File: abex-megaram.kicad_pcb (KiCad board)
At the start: 2 copper layers, 135.5 x 71.5 mm, 54 parts, among them P1 0877159106, P2 CONN_01X01, P3 CONN_01X01, P4 CONN_01X01, P5 CONN_01X01, P6 CONN_01X01, SW2 SW_Push, U1 74HC04, U14 STM32F407VGTx, U7 ISSI61WV5128BL, U8 ISSI61WV5128BL

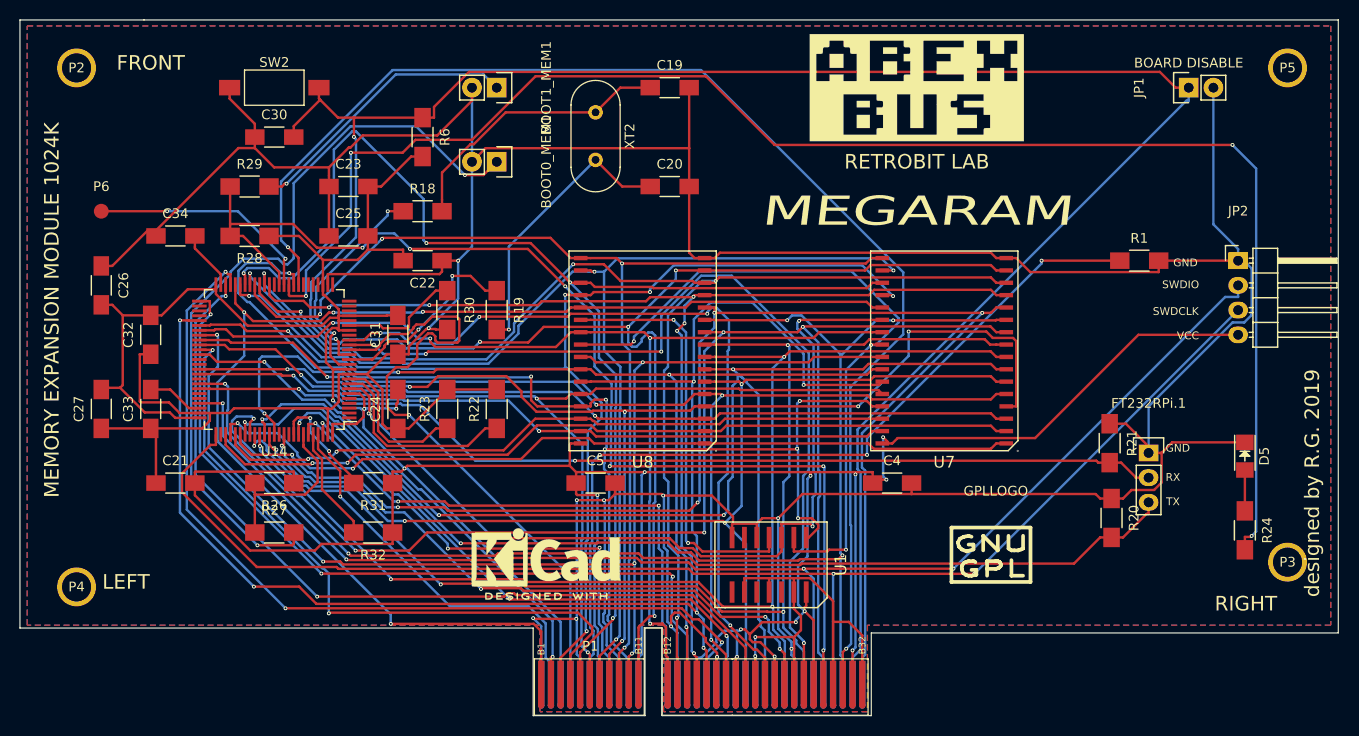
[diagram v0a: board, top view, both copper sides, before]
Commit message: Added a three channel dip-switch for select configuration
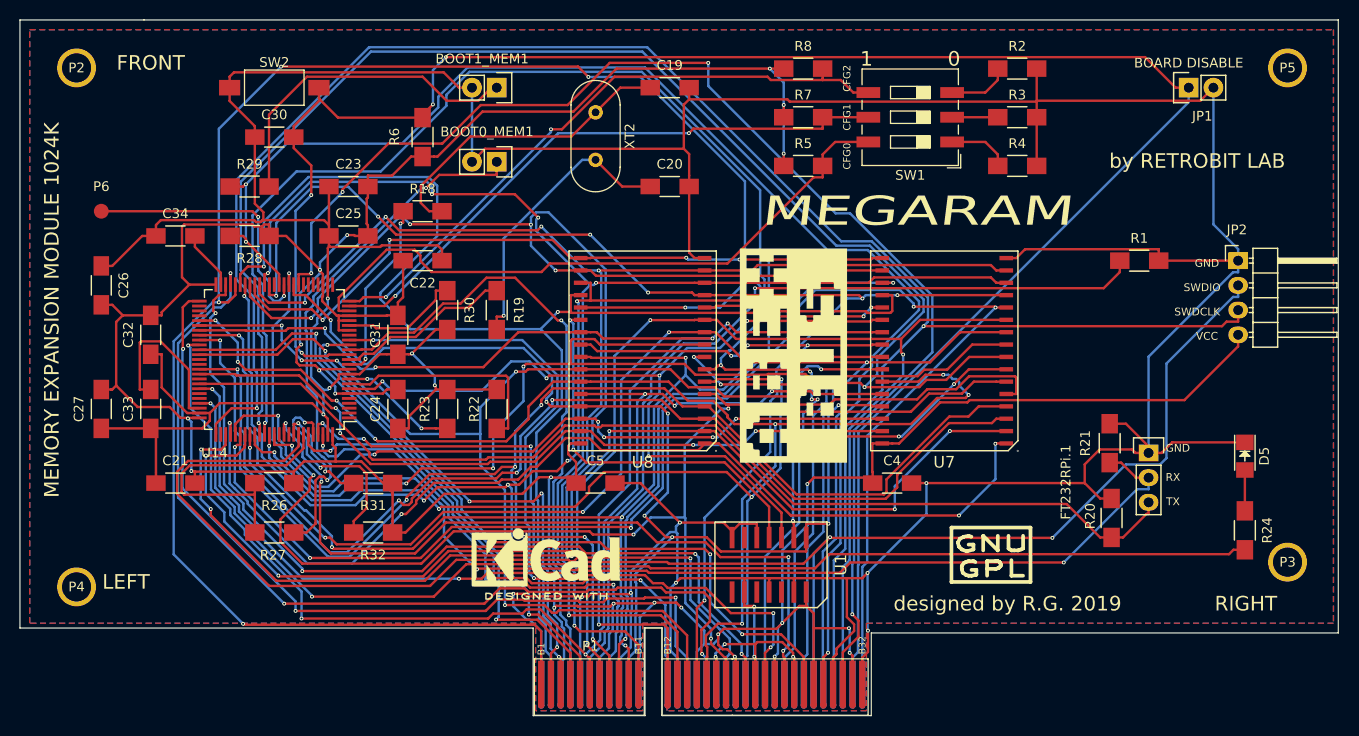
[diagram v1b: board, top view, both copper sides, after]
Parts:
- added R2: 470, Resistors_SMD:R_1206_HandSoldering, F.Cu at (180.5, 59.0)
- added R3: 470, Resistors_SMD:R_1206_HandSoldering, F.Cu at (180.5, 64.0)
- added R4: 470, Resistors_SMD:R_1206_HandSoldering, F.Cu at (180.5, 69.0)
- added R5: 4.7K, Resistors_SMD:R_1206_HandSoldering, F.Cu at (158.5, 69.0)
- added R7: 4.7K, Resistors_SMD:R_1206_HandSoldering, F.Cu at (158.5, 64.0)
- added R8: 4.7K, Resistors_SMD:R_1206_HandSoldering, F.Cu at (158.5, 59.0)
- added SW1: SW_DIP_x03, RetroBitLab:SW_DIP_SPSTx03_Slide_9.78x9.8mm_W8.61mm_P2.54mm, F.Cu at (169.5, 64.0)
- moved ABEXLOGO 30.3 mm to (157.5, 88.5), turned to 90 degrees
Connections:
- U14 pad 23: (no net) -> mCONF0
- U14 pad 24: (no net) -> mCONF1
- U14 pad 25: (no net) -> mCONF2
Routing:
- net mD7: track 131.9 -> 203.6 mm, vias 4 -> 8
- net mCONF0: track 0.00 -> 67.1 mm
- net mA4: track 127.1 -> 193.7 mm, vias 4 -> 5
- net mCONF2: track 0.00 -> 64.9 mm, vias 0 -> 2
- net mCONF1: track 0.00 -> 62.1 mm, vias 0 -> 2
- net SWDCLK: track 142.2 -> 195.1 mm
- net mA5: track 134.7 -> 177.3 mm, vias 4 -> 8
- net LEDGRN_MEM: track 159.8 -> 128.9 mm, vias 4 -> 2
- net mB2: track 84.5 -> 115.3 mm, vias 2 -> 6
- net ~mD1XX: track 60.2 -> 89.8 mm, vias 3 -> 1
- net mB0: track 85.5 -> 113.9 mm, vias 2 -> 4
- net mRD5: track 116.2 -> 143.6 mm, vias 6 -> 3
- net mA13: track 104.7 -> 130.3 mm, vias 3 -> 6
- net Net-(BOOT0_MEM1-Pad1): track 78.7 -> 54.4 mm
- net mD6: track 118.7 -> 142.4 mm, vias 5 -> 3
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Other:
- board text added: "0"
- board text added: "1"
- board text added: "CFG0"
- board text added: "CFG1"
- board text added: "CFG2"
- board text added: "by RETROBIT LAB"
- board text removed: "RETROBIT LAB"

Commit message: Optimized for 8 bit access. Added a configuration option. A31 on connector is 5VDC. Not used here
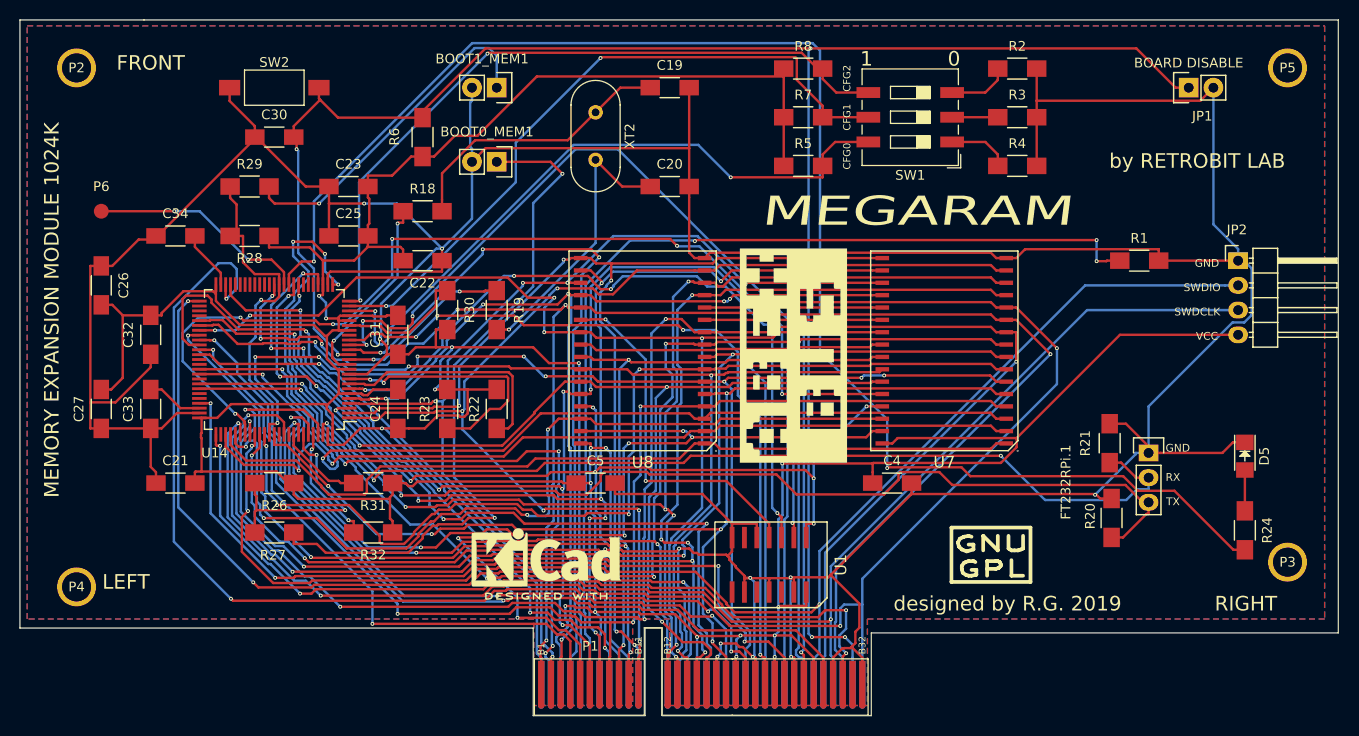
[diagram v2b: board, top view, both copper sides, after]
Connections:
- P1 pad A31: VCC_3V3 -> (no net)
- U14 pad 1: (no net) -> mD2
- U14 pad 2: (no net) -> mD3
- U14 pad 26: (no net) -> ~mRST
- U14 pad 29: (no net) -> ~mREF
- U14 pad 3: (no net) -> mD4
- U14 pad 38: (no net) -> mD7
- U14 pad 39: mD0 -> (no net)
- U14 pad 4: (no net) -> mD5
- U14 pad 40: mD1 -> (no net)
- U14 pad 41: mD2 -> (no net)
- U14 pad 42: mD3 -> (no net)
- U14 pad 43: mD4 -> (no net)
- U14 pad 44: mD5 -> (no net)
- U14 pad 45: mD6 -> (no net)
- U14 pad 46: mD7 -> (no net)
- U14 pad 5: (no net) -> mD6
- U14 pad 97: ~mRST -> mD0
- U14 pad 98: ~mREF -> mD1
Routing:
- net mD7: track 203.6 -> 115.1 mm, vias 8 -> 6
- net SWDCLK: track 195.1 -> 142.2 mm, vias 2 -> 3
- net mA4: track 193.7 -> 144.1 mm
- net GND: track 592.3 -> 641.8 mm, vias 18 -> 16
- net ~mCCTL: track 133.8 -> 87.8 mm
- net mA5: track 177.3 -> 135.4 mm, vias 8 -> 5
- net mD6: track 142.4 -> 101.4 mm, vias 3 -> 6
- net mRD5: track 143.6 -> 104.6 mm, vias 3 -> 2
- net mA2: track 136.3 -> 171.4 mm
- net ~mRST: track 49.2 -> 82.5 mm, vias 3 -> 7
- net ~mS5: track 72.8 -> 102.2 mm
- net mB2: track 115.3 -> 87.5 mm, vias 6 -> 2
- net mB1: track 77.9 -> 105.1 mm, vias 4 -> 6
- net LEDGRN_MEM: track 128.9 -> 155.5 mm
- net mD1: track 143.6 -> 118.5 mm, vias 5 -> 6
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
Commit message: Upgraded to a dual chip select for external SRAM. In this case up to 1536k can be addressable
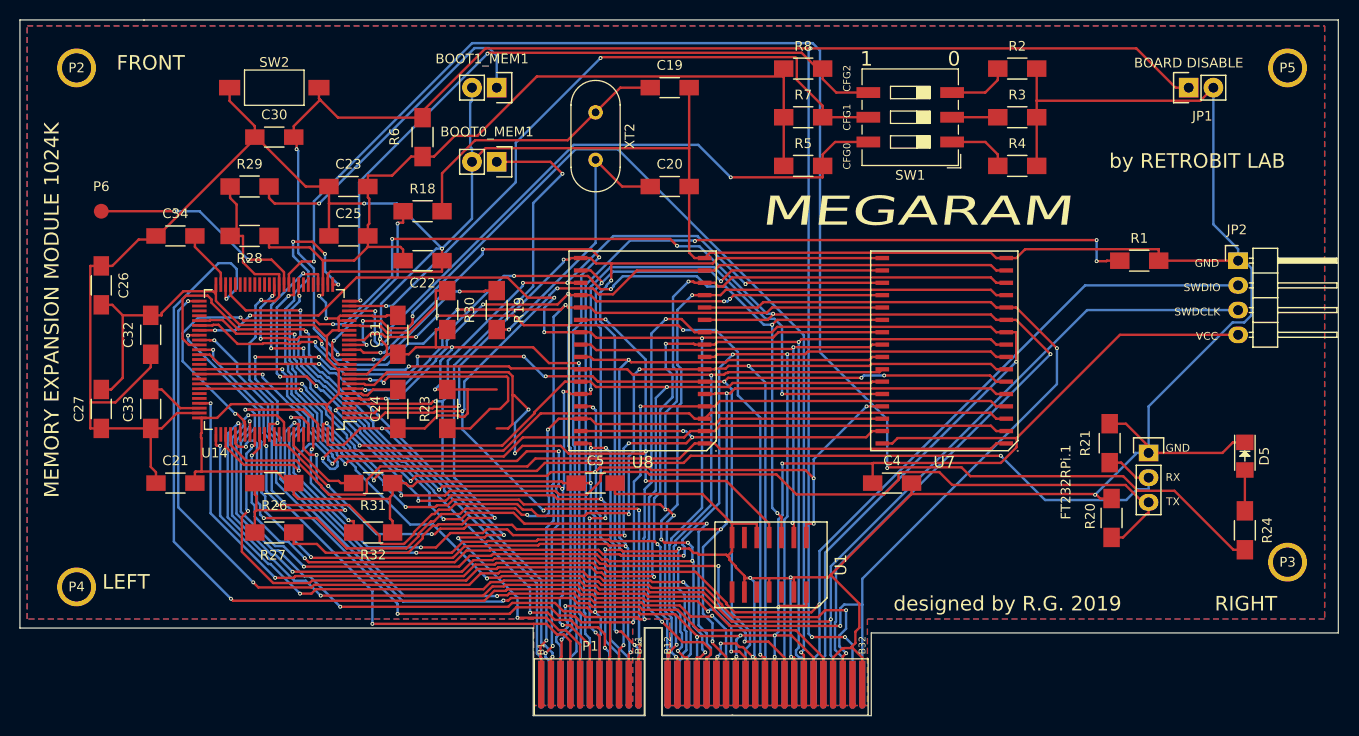
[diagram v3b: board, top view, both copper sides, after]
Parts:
- removed ABEXLOGO: LOGO, RetroBitLab:ABEX_Logo_22mmx11mm_WB
- removed G***: LOGO, RetroBitLab:atari_800_XL_BW_25x25
- removed GPLLOGO: Symbol_GNU-GPL_CopperTop_Small, RetroBitLab:Symbol_GNU-GPL_SilkScreen_Small
- removed KICADLOGO: KiCad-Logo2_6mm_SilkScreen, Symbol:KiCad-Logo2_6mm_SilkScreen
- removed R22: 0, Resistors_SMD:R_1206_HandSoldering
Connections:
- U1 pad 3: mB5 -> GND
- U1 pad 4: ~mB5 -> (no net)
- U14 pad 7: mB5 -> mCS_512K
- U14 pad 8: mB6 -> mCS_1024K
- U7 pad 22: mB5 -> mCS_512K
- U8 pad 22: ~mB5 -> mCS_1024K
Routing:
- net mB5: track 86.1 -> 0.00 mm, vias 5 -> 0
- net mCS_512K: track 0.00 -> 83.4 mm, vias 0 -> 4
- net mCS_1024K: track 0.00 -> 82.7 mm, vias 0 -> 5
- net ~mB5: track 36.8 -> 0.00 mm, vias 2 -> 0
- net mB6: track 24.3 -> 0.00 mm
- net GND: track 641.8 -> 644.5 mm, vias 16 -> 17

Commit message: Added nOE and nWE from the GPIOs
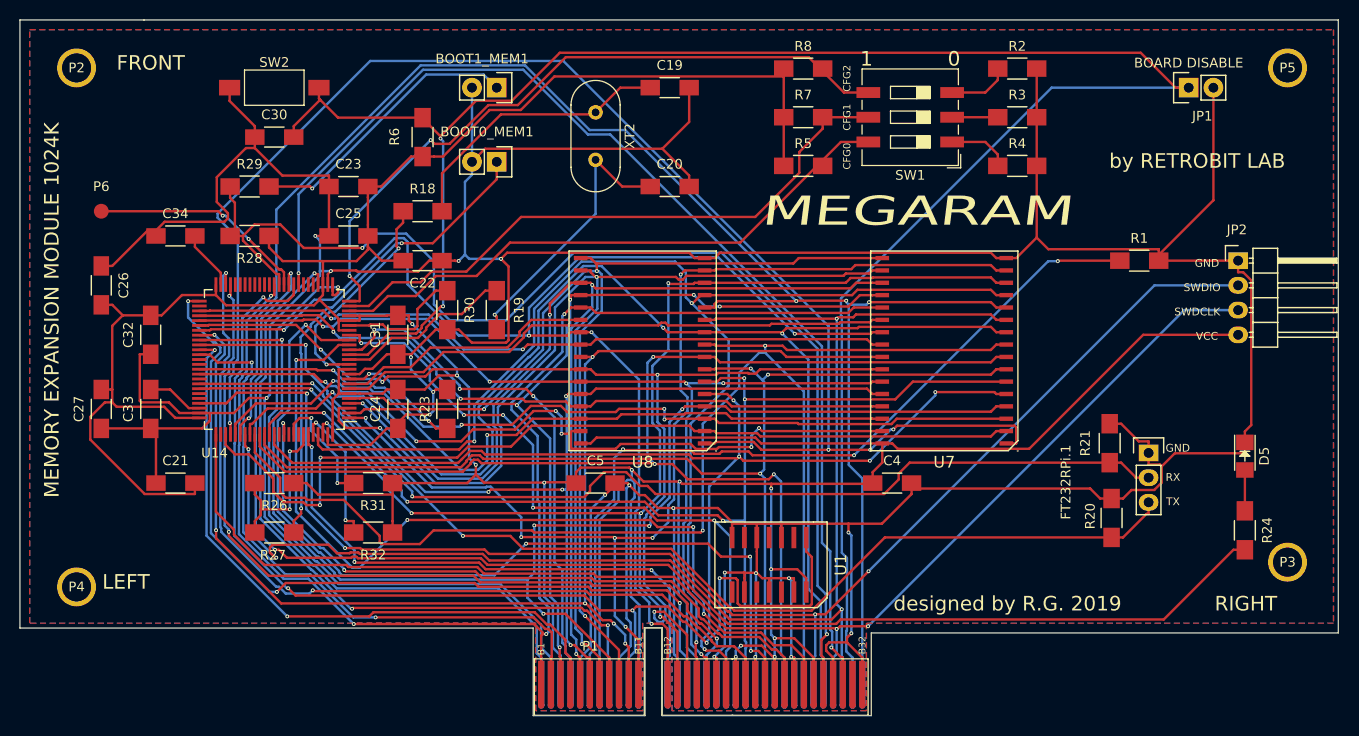
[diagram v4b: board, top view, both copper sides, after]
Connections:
- U1 pad 2: mW/~R -> (no net)
- U14 pad 18: (no net) -> ~mD1XX
- U14 pad 53: (no net) -> mOE
- U14 pad 54: (no net) -> mWE
- U14 pad 93: ~mD1XX -> (no net)
- U7 pad 24: mW/~R -> mOE
- U7 pad 29: mR/~W -> mWE
- U8 pad 24: mW/~R -> mOE
- U8 pad 29: mR/~W -> mWE
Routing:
- net mWE: track 0.00 -> 75.0 mm, vias 0 -> 2
- net mOE: track 0.00 -> 72.9 mm, vias 0 -> 2
- net mB3: track 86.4 -> 153.4 mm, vias 0 -> 4
- net mCS_1024K: track 82.7 -> 26.7 mm, vias 5 -> 0
- net VCC_3V3: track 430.0 -> 484.2 mm, vias 16 -> 12
- net mW/~R: track 51.2 -> 0.00 mm, vias 2 -> 0
- net mA13: track 142.0 -> 109.8 mm, vias 7 -> 5
- net mA2: track 171.3 -> 141.2 mm, vias 5 -> 3
- net ~mCCTL: track 87.8 -> 115.8 mm, vias 4 -> 2
- net mCS_512K: track 83.4 -> 58.2 mm, vias 4 -> 0
- net mB1: track 105.1 -> 81.2 mm
- net Net-(BOOT0_MEM1-Pad1): track 72.8 -> 49.2 mm
- net mD7: track 115.1 -> 138.6 mm, vias 6 -> 4
- net mPHI2: track 76.1 -> 54.4 mm
- net SWDRST: track 196.6 -> 216.4 mm, vias 5 -> 2
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
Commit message: New layout and design
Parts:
- removed C26, C27, C30, C31: 100n, Capacitors_SMD:C_1206_HandSoldering
- removed C32: 1u, Capacitors_SMD:C_1206_HandSoldering
- removed C33, C34: 2.2u, Capacitors_SMD:C_1206_HandSoldering
- removed D5: LED.GREEN, LEDs:LED_1206
- removed P6: CONN_01X01, Measurement_Points:Measurement_Point_Round-SMD-Pad_Small
- removed R21, R26, R28: 10K, Resistors_SMD:R_1206_HandSoldering
- removed R23, R30: 0, Resistors_SMD:R_1206_HandSoldering
- removed R24: 220, Resistors_SMD:R_1206_HandSoldering
- removed R27, R29: 510, Resistors_SMD:R_1206_HandSoldering
- removed R31, R32: 4.7K, Resistors_SMD:R_1206_HandSoldering
- removed U14: STM32F407VGTx, Housings_QFP:TQFP-100_14x14mm_Pitch0.5mm
- removed U7, U8: ISSI61WV5128BL, RetroBitLab:SOP-32L-20.5x11.30-1.27mm
- removed XT2: 8Mhz, RetroBitLab:Crystal_HC49-4H_Vertical_3D
- added C1: 100n, Capacitors_SMD:C_1206_HandSoldering, F.Cu at (167.0, 64.0)
- added C10: 100n, Capacitors_SMD:C_1206_HandSoldering, F.Cu at (125.0, 70.0)
- added C11: 100n, Capacitors_SMD:C_1206_HandSoldering, F.Cu at (134.0, 68.0)
- added C12: 100n, Capacitors_SMD:C_1206_HandSoldering, F.Cu at (143.0, 68.0)
- added C13: 100n, Capacitors_SMD:C_1206_HandSoldering, F.Cu at (151.0, 68.0)
- added C14: 100n, Capacitors_SMD:C_1206_HandSoldering, F.Cu at (160.0, 70.0)
- added C15: 100n, Capacitors_SMD:C_1206_HandSoldering, F.Cu at (160.0, 78.0)
- added C16: 100n, Capacitors_SMD:C_1206_HandSoldering, F.Cu at (160.0, 86.0)
- added C17: 100n, Capacitors_SMD:C_1206_HandSoldering, F.Cu at (160.0, 94.0)
- added C18: 100n, Capacitors_SMD:C_1206_HandSoldering, F.Cu at (160.0, 101.0)
- added C2: 100n, Capacitors_SMD:C_1206_HandSoldering, F.Cu at (185.0, 72.0)
- added C3: 100n, Capacitors_SMD:C_1206_HandSoldering, F.Cu at (102.0, 71.0)
- added C6: 20p, Capacitors_SMD:C_1206_HandSoldering, F.Cu at (111.0, 92.0)
- added C7: 20p, Capacitors_SMD:C_1206_HandSoldering, F.Cu at (111.0, 84.0)
- added C8: 100n, Capacitors_SMD:C_1206_HandSoldering, F.Cu at (124.0, 92.0)
- added C9: 1u, Capacitors_SMD:C_1206_HandSoldering, F.Cu at (117.0, 74.0)
- added D1: LED.GREEN, LEDs:LED_1206, F.Cu at (178.0, 107.0)
- added G***: LOGO, RetroBitLab:ABEX_Logo_22mmx11mm_WB, F.Cu at (99.0, 102.0)
- added R10: 220, Resistors_SMD:R_1206_HandSoldering, F.Cu at (117.0, 79.0)
- added R11: 10K, Resistors_SMD:R_1206_HandSoldering, F.Cu at (136.0, 58.0)
- added R12: 510, Resistors_SMD:R_1206_HandSoldering, F.Cu at (144.0, 58.0)
- added R13: 0, Resistors_SMD:R_1206_HandSoldering, F.Cu at (124.0, 85.0)
- added R14: 10K, Resistors_SMD:R_1206_HandSoldering, F.Cu at (202.0, 104.0)
- added R15: 10K, Resistors_SMD:R_1206_HandSoldering, F.Cu at (115.0, 110.0)
- added R16: 510, Resistors_SMD:R_1206_HandSoldering, F.Cu at (119.0, 110.0)
- added R17: 10K, Resistors_SMD:R_1206_HandSoldering, F.Cu at (202.0, 98.0)
- added R9: 0, Resistors_SMD:R_1206_HandSoldering, F.Cu at (117.0, 98.0)
- added U2: ISSI61WV5128BL, RetroBitLab:SOP-32L-20.5x11.30-1.27mm, F.Cu at (98.0, 85.0)
- added U3: STM32F407IGTx, Housings_QFP:LQFP-176_24x24mm_Pitch0.5mm, F.Cu at (141.0, 87.0)
- added XT1: 8Mhz, RetroBitLab:Crystal_HC49-4H_Vertical_3D, F.Cu at (117.0, 91.0)
- C19, C20: value 20p -> 100n
- C4, C5: value 100n -> 2.2u
- R1: value 0 -> 100K
- R18: value 0 -> 4.7K
- R19: value 220 -> 4.7K
- R2: value 470 -> 0
- R20: value 10K -> 220
- R5: value 4.7K -> 470
- R6: value 100K -> 4.7K
- SW1: value SW_DIP_x03 -> SW_Push; footprint RetroBitLab:SW_DIP_SPSTx03_Slide_9.78x9.8mm_W8.61mm_P2.54mm -> RetroBitLab:SW_SPST_FSMSM_3D
- SW2: value SW_Push -> SW_DIP_x03; footprint RetroBitLab:SW_SPST_FSMSM_3D -> RetroBitLab:SW_DIP_SPSTx03_Slide_9.78x9.8mm_W8.61mm_P2.54mm
- U1: value 74HC04 -> ISSI61WV5128BL; footprint RetroBitLab:PSOP14-5x7.40-1.27 -> RetroBitLab:SOP-32L-20.5x11.30-1.27mm
- moved R2 100.9 mm to (94.0, 111.0), turned to 90 degrees
- moved R4 87.8 mm to (93.0, 62.0), turned to 180 degrees
- moved R3 87.5 mm to (93.0, 66.0), turned to 180 degrees
- moved R5 66.4 mm to (93.0, 58.0), turned to 180 degrees
- moved BOOT1_MEM1 49.0 mm to (127.0, 110.0)
- moved C19 44.6 mm to (152.0, 105.0), turned to 180 degrees
- moved R8 44.1 mm to (115.0, 66.0), turned to 180 degrees
- moved R7 43.5 mm to (115.0, 62.0), turned to 180 degrees
- moved C21 42.2 mm to (136.0, 105.0), turned to 180 degrees
- moved U1 35.4 mm to (181.0, 86.0), turned to 270 degrees
- moved C20 33.9 mm to (144.0, 105.0)
- moved C23 32.5 mm to (118.0, 103.0), turned to 180 degrees
- moved BOOT0_MEM1 28.1 mm to (153.0, 58.0)
- moved C22 26.1 mm to (126.0, 104.0), turned to 0 degrees
- moved R1 25.6 mm to (178.0, 58.0)
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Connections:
- C19 pad 1: Net-(C19-Pad1) -> GND
- C19 pad 2: GND -> VCC_3V3
- C20 pad 1: Net-(C20-Pad1) -> GND
- C20 pad 2: GND -> VCC_3V3
- C4 pad 1: VCC_3V3 -> GND
- C4 pad 2: GND -> VCAP_2_MEM
- C5 pad 1: VCC_3V3 -> GND
- C5 pad 2: GND -> VCAP_1_MEM
- R1 pad 1: mAUDIO -> SWDRST
- R1 pad 2: GND -> VCC_3V3
- R18 pad 1: Net-(R18-Pad1) -> VCC_3V3
- R18 pad 2: Net-(C19-Pad1) -> PB6
- R19 pad 1: Net-(R19-Pad1) -> VCC_3V3
- R19 pad 2: Net-(C20-Pad1) -> PB9
- R2 pad 1: Net-(R2-Pad1) -> mAUDIO
- R20 pad 1: GND -> Net-(D1-Pad2)
- R20 pad 2: UART_TX -> LEDGRN_MEM
- R5 pad 1: VCC_3V3 -> Net-(R5-Pad1)
- R5 pad 2: mCONF0 -> GND
- R6 pad 1: SWDRST -> VCC_3V3
- R6 pad 2: VCC_3V3 -> mCONF0
- SW1 pad 1: Net-(R4-Pad1) -> GND
- SW1 pad 2: Net-(R3-Pad1) -> SWDRST
- SW2 pad 1: GND -> Net-(R5-Pad1)
- SW2 pad 2: SWDRST -> Net-(R4-Pad1)
- U1 pad 1: mR/~W -> FSMC_A17
- U1 pad 10: (no net) -> FSMC_A2
- U1 pad 11: GND -> FSMC_A1
- U1 pad 12: (no net) -> FSMC_A0
- U1 pad 13: GND -> FSMC_D0
- U1 pad 14: VCC_3V3 -> FSMC_D1
- U1 pad 2: (no net) -> FSMC_A16
- U1 pad 3: GND -> FSMC_A14
- U1 pad 4: (no net) -> FSMC_A12
- U1 pad 5: GND -> FSMC_A7
- U1 pad 6: (no net) -> FSMC_A6
- U1 pad 7: GND -> FSMC_A5
- U1 pad 8: (no net) -> FSMC_A4
- U1 pad 9: GND -> FSMC_A3
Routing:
- net FSMC_A11: track 0.00 -> 194.5 mm, vias 0 -> 5
- net FSMC_D4: track 0.00 -> 190.5 mm, vias 0 -> 7
- net FSMC_D0: track 0.00 -> 164.0 mm, vias 0 -> 8
- net FSMC_A10: track 0.00 -> 155.6 mm, vias 0 -> 9
- net FSMC_A9: track 0.00 -> 154.4 mm, vias 0 -> 5
- net mB3: track 153.4 -> 0.00 mm, vias 4 -> 0
- net FSMC_D3: track 0.00 -> 152.0 mm, vias 0 -> 3
- net FSMC_A13: track 0.00 -> 150.9 mm, vias 0 -> 7
- net FSMC_A16: track 0.00 -> 144.5 mm, vias 0 -> 9
- net FSMC_A8: track 0.00 -> 141.0 mm, vias 0 -> 5
- net FSMC_A15: track 0.00 -> 136.1 mm, vias 0 -> 10
- net FSMC_NOE: track 0.00 -> 131.4 mm, vias 0 -> 5
- net FSMC_A14: track 0.00 -> 130.5 mm, vias 0 -> 5
- net FSMC_D1: track 0.00 -> 128.8 mm, vias 0 -> 8
- net FSMC_A7: track 0.00 -> 128.6 mm, vias 0 -> 5
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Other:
- board text removed: "0"
- board text removed: "1"
- board text removed: "CFG0"
- board text removed: "CFG1"
- board text removed: "CFG2"
- board text removed: "FRONT"
